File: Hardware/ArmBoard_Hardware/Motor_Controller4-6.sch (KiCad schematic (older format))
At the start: 27 parts

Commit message: ENx_# Updated
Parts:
- R?: value 3.3k -> 3.3
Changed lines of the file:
@@
 AR Path="/63845FEF/637AF810" Ref="R?"  Part="1"
 F 0 "R?" H 2559 4796 50  0000 L CNN
-F 1 "3.3k" H 2559 4705 50  0000 L CNN
+F 1 "3.3" H 2559 4705 50  0000 L CNN
 F 2 "" H 2500 4750 50  0001 C CNN
 F 3 "~" H 2500 4750 50  0001 C CNN

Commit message: Added MotorToggles
Removed extra schematic files, added a MotorToggle sheet for the toggle buttons, sheet docs were updated
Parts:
- gave numbers to parts that had none: 27

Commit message: need to change the mosfet and the other footrpints under it
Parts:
- R75: renamed from R68; footprint (none) -> Resistor_SMD:R_0603_1608Metric_Pad0.98x0.95mm_HandSolder
- R76: renamed from R69; footprint (none) -> Resistor_SMD:R_0603_1608Metric_Pad0.98x0.95mm_HandSolder
- R77: renamed from R70; footprint (none) -> Resistor_SMD:R_0603_1608Metric_Pad0.98x0.95mm_HandSolder
- R78: renamed from R71; footprint (none) -> Resistor_SMD:R_0603_1608Metric_Pad0.98x0.95mm_HandSolder
- R79: renamed from R72; footprint (none) -> Resistor_SMD:R_0603_1608Metric_Pad0.98x0.95mm_HandSolder
- R80: renamed from R73; footprint (none) -> Resistor_SMD:R_0603_1608Metric_Pad0.98x0.95mm_HandSolder
- R81: renamed from R74; footprint (none) -> Resistor_SMD:R_0603_1608Metric_Pad0.98x0.95mm_HandSolder
- R82: renamed from R75; footprint (none) -> Resistor_SMD:R_0603_1608Metric_Pad0.98x0.95mm_HandSolder
- R83: renamed from R76; footprint (none) -> Resistor_SMD:R_0603_1608Metric_Pad0.98x0.95mm_HandSolder
- R84: renamed from R77; footprint (none) -> Resistor_SMD:R_0603_1608Metric_Pad0.98x0.95mm_HandSolder
- R85: renamed from R78; footprint (none) -> Resistor_SMD:R_0603_1608Metric_Pad0.98x0.95mm_HandSolder
- R86: renamed from R79; footprint (none) -> Resistor_SMD:R_0603_1608Metric_Pad0.98x0.95mm_HandSolder
- R87: renamed from R80; footprint (none) -> Resistor_SMD:R_0603_1608Metric_Pad0.98x0.95mm_HandSolder
- R88: renamed from R81; footprint (none) -> Resistor_SMD:R_0603_1608Metric_Pad0.98x0.95mm_HandSolder
- R89: renamed from R82; footprint (none) -> Resistor_SMD:R_0603_1608Metric_Pad0.98x0.95mm_HandSolder
- R90: renamed from R83; footprint (none) -> Resistor_SMD:R_0603_1608Metric_Pad0.98x0.95mm_HandSolder
- R91: renamed from R84; footprint (none) -> Resistor_SMD:R_0603_1608Metric_Pad0.98x0.95mm_HandSolder
- R92: renamed from R85; footprint (none) -> Resistor_SMD:R_0603_1608Metric_Pad0.98x0.95mm_HandSolder
- R93: renamed from R86; footprint (none) -> Resistor_SMD:R_0603_1608Metric_Pad0.98x0.95mm_HandSolder
- R94: renamed from R87; footprint (none) -> Resistor_SMD:R_0603_1608Metric_Pad0.98x0.95mm_HandSolder
- R95: renamed from R88; footprint (none) -> Resistor_SMD:R_0603_1608Metric_Pad0.98x0.95mm_HandSolder
- U6: renamed from U7; footprint (none) -> MRDT_ICs:MultiPowerSO_30
- U7: renamed from U8; footprint (none) -> MRDT_ICs:MultiPowerSO_30
- U8: renamed from U9; footprint (none) -> MRDT_ICs:MultiPowerSO_30
- renumbered Q35 to Q34, Q36 to Q35, Q37 to Q36

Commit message: late night with the boy
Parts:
- removed Q34, Q35, Q36: BUK7M6R3-40EX, Package_TO_SOT_SMD:LFPAK33, symbol Transistor_FET:BUK7M6R3-40EX
- removed R75, R76, R77, R78, R79, R80, R81, R82, R83, R86, R88, R89, R90, R91, R92: 1k, Resistor_SMD:R_0603_1608Metric_Pad0.98x0.95mm_HandSolder, symbol Device:R_Small
- removed R84, R87, R93, R94, R95: 3.3k, Resistor_SMD:R_0603_1608Metric_Pad0.98x0.95mm_HandSolder, symbol Device:R_Small
- removed R85: 3.3, Resistor_SMD:R_0603_1608Metric_Pad0.98x0.95mm_HandSolder, symbol Device:R_Small
- removed U6, U7, U8: VNH5019A_E, MRDT_ICs:MultiPowerSO_30, symbol ArmBoard_Hardware-rescue:VNH5019A_E-MRDT_ICs
- added C10, C8, C9: C_Small, Capacitor_SMD:C_0603_1608Metric_Pad1.08x0.95mm_HandSolder, symbol Device:C_Small
- added R49, R50, R55: 20k, Resistor_SMD:R_0603_1608Metric_Pad0.98x0.95mm_HandSolder, symbol Device:R
- added R51, R52, R53, R54, R56, R57: 1k, Resistor_SMD:R_0603_1608Metric_Pad0.98x0.95mm_HandSolder, symbol Device:R_Small
- added U10, U11, U14: LTC6900, Package_TO_SOT_SMD:SOT-23-5_HandSoldering, symbol MRDT_Devices:LTC6900
- added U12, U13, U15: TB67H400AFNG,EL, MRDT_ICs:TB67H400AFNG,EL, symbol MRDT_ICs:TB67H400AFNG,EL
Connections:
- net labels added: +5V
- net labels removed: +3.3V, ENa_4, ENa_5, ENa_6, ENb_4, ENb_5, ENb_6
- wire segments 228 -> 165
- no-connect marks 0 -> 12

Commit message: Fixed Oscillators
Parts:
- U10, U11, U14: symbol MRDT_Devices:LTC6900 -> ArmBoard_Hardware-rescue:LTC6900-MRDT_Devices
- U12, U13, U15: symbol MRDT_ICs:TB67H400AFNG,EL -> ArmBoard_Hardware-rescue:TB67H400AFNG,EL-MRDT_ICs
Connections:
- net +5V: now also R49.1, R50.1, R55.1
- net GND: now also C10.2, C8.2, C9.2
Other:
- moved on the sheet: C10, C8, C9
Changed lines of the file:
@@
 IN_A_4
 $Comp
-L MRDT_ICs:TB67H400AFNG,EL U?
+L ArmBoard_Hardware-rescue:TB67H400AFNG,EL-MRDT_ICs U?
 U 1 1 624C6CB1
 P 3160 2365
@@
 	2135 1415 2360 1415
 $Comp
-L MRDT_Devices:LTC6900 U?
+L ArmBoard_Hardware-rescue:LTC6900-MRDT_Devices U?
 U 1 1 624C6C60
 P 1430 975
 AR Path="/63845F20/624C6C60" Ref="U?"  Part="1"
 AR Path="/63845FEF/624C6C60" Ref="U10"  Part="1"
+AR Path="/624C6C60" Ref="U10"  Part="1"
 F 0 "U10" H 1500 1260 50  0000 C CNN
 F 1 "LTC6900" H 1500 1169 50  0000 C CNN
@@
 L Device:C_Small C?
 U 1 1 624C6C44
-P 795 865
+P 675 865
 AR Path="/63845F20/624C6C44" Ref="C?"  Part="1"
 AR Path="/63845FEF/624C6C44" Ref="C8"  Part="1"
-F 0 "C8" H 887 911 50  0000 L CNN
-F 1 "C_Small" H 887 820 50  0000 L CNN
-F 2 "Capacitor_SMD:C_0603_1608Metric_Pad1.08x0.95mm_HandSolder" H 795 865 50  0001 C CNN
-F 3 "~" H 795 865 50  0001 C CNN
-	1    795  865
-	1    0    0    -1
-$EndComp
-Wire Wire Line
-	795  965  795  1115
+F 0 "C8" H 767 911 50  0000 L CNN
+F 1 "C_Small" H 767 820 50  0000 L CNN
+F 2 "Capacitor_SMD:C_0603_1608Metric_Pad1.08x0.95mm_HandSolder" H 675 865 50  0001 C CNN
+F 3 "~" H 675 865 50  0001 C CNN
+	1    675  865
+	1    0    0    -1
+$EndComp
 Wire Wire Line
 	795  1115 800  1115
@@
 Wire Wire Line
 	5950 1105 5955 1105
-Wire Wire Line
-	5950 955  5950 1105
 $Comp
 L Device:C_Small C?
 U 1 1 6250A179
-P 5950 855
+P 5830 865
 AR Path="/63845F20/6250A179" Ref="C?"  Part="1"
 AR Path="/63845FEF/6250A179" Ref="C10"  Part="1"
-F 0 "C10" H 6042 901 50  0000 L CNN
-F 1 "C_Small" H 6042 810 50  0000 L CNN
-F 2 "Capacitor_SMD:C_0603_1608Metric_Pad1.08x0.95mm_HandSolder" H 5950 855 50  0001 C CNN
-F 3 "~" H 5950 855 50  0001 C CNN
-	1    5950 855
+F 0 "C10" H 5922 911 50  0000 L CNN
+F 1 "C_Small" H 5922 820 50  0000 L CNN
+F 2 "Capacitor_SMD:C_0603_1608Metric_Pad1.08x0.95mm_HandSolder" H 5830 865 50  0001 C CNN
+F 3 "~" H 5830 865 50  0001 C CNN
+	1    5830 865
 	1    0    0    -1
 $EndComp
@@
 	6975 1005 7515 1005
 $Comp
-L MRDT_Devices:LTC6900 U?
+L ArmBoard_Hardware-rescue:LTC6900-MRDT_Devices U?
 U 1 1 6250A195
 P 6585 965
 AR Path="/63845F20/6250A195" Ref="U?"  Part="1"
 AR Path="/63845FEF/6250A195" Ref="U14"  Part="1"
+AR Path="/6250A195" Ref="U14"  Part="1"
 F 0 "U14" H 6655 1250 50  0000 C CNN
 F 1 "LTC6900" H 6655 1159 50  0000 C CNN
@@
 	8315 3905 8315 3780
 $Comp
-L MRDT_ICs:TB67H400AFNG,EL U?
+L ArmBoard_Hardware-rescue:TB67H400AFNG,EL-MRDT_ICs U?
 U 1 1 6250A1E6
 P 8315 2355
@@
 	1160 4480 1160 4445
 Wire Wire Line
-	950  4480 1160 4480
-Wire Wire Line
 	1335 4480 1335 4630
 $Comp
@@
 Wire Wire Line
 	950  4830 955  4830
-Wire Wire Line
-	950  4680 950  4830
 $Comp
 L Device:C_Small C?
 U 1 1 62512C8B
-P 950 4580
+P 830 4585
 AR Path="/63845F20/62512C8B" Ref="C?"  Part="1"
 AR Path="/63845FEF/62512C8B" Ref="C9"  Part="1"
-F 0 "C9" H 1042 4626 50  0000 L CNN
-F 1 "C_Small" H 1042 4535 50  0000 L CNN
-F 2 "Capacitor_SMD:C_0603_1608Metric_Pad1.08x0.95mm_HandSolder" H 950 4580 50  0001 C CNN
-F 3 "~" H 950 4580 50  0001 C CNN
-	1    950  4580
+F 0 "C9" H 922 4631 50  0000 L CNN
+F 1 "C_Small" H 922 4540 50  0000 L CNN
+F 2 "Capacitor_SMD:C_0603_1608Metric_Pad1.08x0.95mm_HandSolder" H 830 4585 50  0001 C CNN
+F 3 "~" H 830 4585 50  0001 C CNN
+	1    830  4585
 	1    0    0    -1
 $EndComp
@@
 	1975 4730 2515 4730
 $Comp
-L MRDT_Devices:LTC6900 U?
+L ArmBoard_Hardware-rescue:LTC6900-MRDT_Devices U?
 U 1 1 62512CA7
 P 1585 4690
 AR Path="/63845F20/62512CA7" Ref="U?"  Part="1"
 AR Path="/63845FEF/62512CA7" Ref="U11"  Part="1"
+AR Path="/62512CA7" Ref="U11"  Part="1"
 F 0 "U11" H 1655 4975 50  0000 C CNN
 F 1 "LTC6900" H 1655 4884 50  0000 C CNN
@@
 	3315 7630 3315 7505
 $Comp
-L MRDT_ICs:TB67H400AFNG,EL U?
+L ArmBoard_Hardware-rescue:TB67H400AFNG,EL-MRDT_ICs U?
 U 1 1 62512CF8
 P 3315 6080
@@
 Text GLabel 2365 6925 0    50   Output ~ 0
 OUTa_6
+Wire Wire Line
+	675  965  675  1015
+Wire Wire Line
+	795  765  795  1115
+Wire Wire Line
+	675  765  795  765
+Connection ~ 795  765
+Wire Wire Line
+	830  4485 830  4480
+Wire Wire Line
+	830  4480 950  4480
+Wire Wire Line
+	950  4480 950  4830
+Connection ~ 950  4480
+Wire Wire Line
+	950  4480 1160 4480
+Wire Wire Line
+	830  4685 830  4730
+Connection ~ 830  4730
+Connection ~ 675  1015
+Wire Wire Line
+	5830 765  5830 755
+Wire Wire Line
+	5830 755  5950 755
+Wire Wire Line
+	5950 755  5950 1105
+Connection ~ 5950 755
+Wire Wire Line
+	5830 965  5830 1005
+Connection ~ 5830 1005
 $EndSCHEMATC

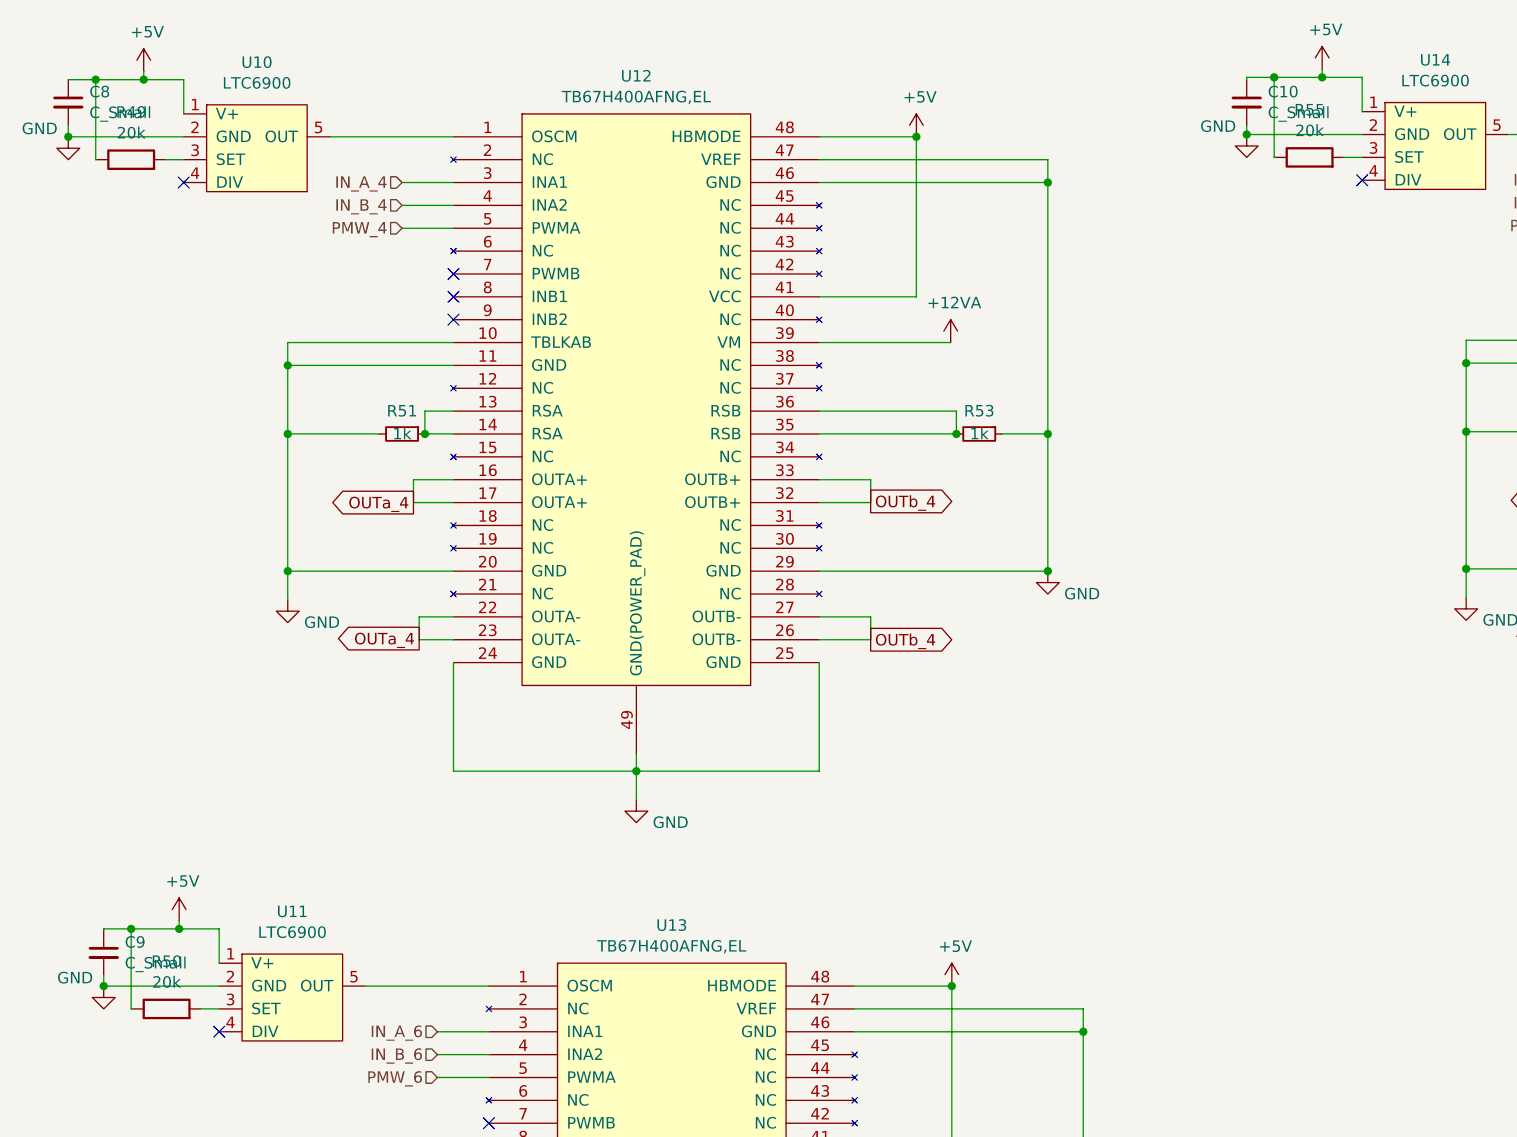
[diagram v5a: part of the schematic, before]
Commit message: Worked on Motor Drivers
added major tracing of motor drivers
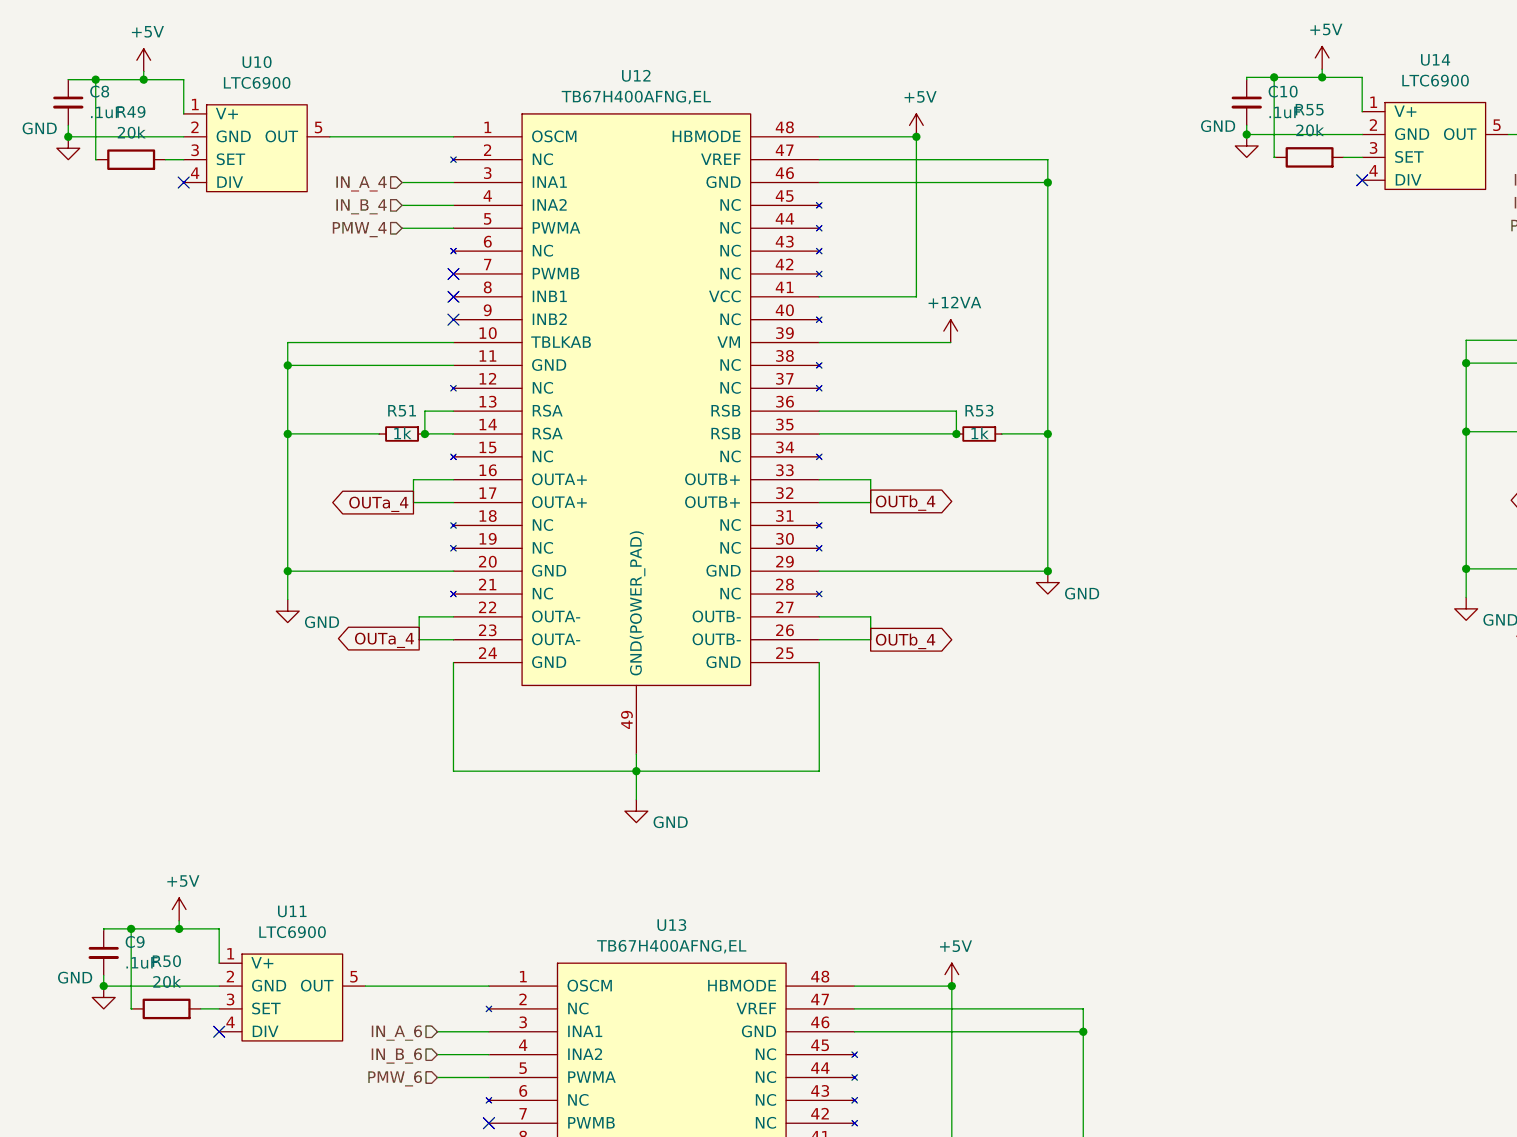
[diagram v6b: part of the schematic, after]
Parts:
- C10, C8, C9: value C_Small -> .1uF
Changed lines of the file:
@@
 AR Path="/63845FEF/624C6C44" Ref="C8"  Part="1"
 F 0 "C8" H 767 911 50  0000 L CNN
-F 1 "C_Small" H 767 820 50  0000 L CNN
+F 1 ".1uF" H 767 820 50  0000 L CNN
 F 2 "Capacitor_SMD:C_0603_1608Metric_Pad1.08x0.95mm_HandSolder" H 675 865 50  0001 C CNN
 F 3 "~" H 675 865 50  0001 C CNN
@@
 AR Path="/63845FEF/6250A179" Ref="C10"  Part="1"
 F 0 "C10" H 5922 911 50  0000 L CNN
-F 1 "C_Small" H 5922 820 50  0000 L CNN
+F 1 ".1uF" H 5922 820 50  0000 L CNN
 F 2 "Capacitor_SMD:C_0603_1608Metric_Pad1.08x0.95mm_HandSolder" H 5830 865 50  0001 C CNN
 F 3 "~" H 5830 865 50  0001 C CNN
@@
 AR Path="/63845FEF/62512C8B" Ref="C9"  Part="1"
 F 0 "C9" H 922 4631 50  0000 L CNN
-F 1 "C_Small" H 922 4540 50  0000 L CNN
+F 1 ".1uF" H 922 4540 50  0000 L CNN
 F 2 "Capacitor_SMD:C_0603_1608Metric_Pad1.08x0.95mm_HandSolder" H 830 4585 50  0001 C CNN
 F 3 "~" H 830 4585 50  0001 C CNN

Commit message: armboard review
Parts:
- removed C10, C8, C9: .1uF, Capacitor_SMD:C_0603_1608Metric_Pad1.08x0.95mm_HandSolder, symbol Device:C_Small
- removed R49, R50, R55: 20k, Resistor_SMD:R_0603_1608Metric_Pad0.98x0.95mm_HandSolder, symbol Device:R
- removed U10, U11, U14: LTC6900, Package_TO_SOT_SMD:SOT-23-5_HandSoldering, symbol ArmBoard_Hardware-rescue:LTC6900-MRDT_Devices
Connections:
- net OSC: now reaches U12.1 (OSCM)
- net OSC: now also U13.1 (OSCM), U15.1 (OSCM)
- no-connect marks 12 -> 9

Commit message: Rescued the Libaries
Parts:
- U12, U13, U15: symbol ArmBoard_Hardware-rescue:TB67H400AFNG,EL-MRDT_ICs -> MRDT_ICs:TB67H400AFNG,EL
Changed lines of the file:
@@
 IN_A_4
 $Comp
-L ArmBoard_Hardware-rescue:TB67H400AFNG,EL-MRDT_ICs U?
+L MRDT_ICs:TB67H400AFNG,EL U?
 U 1 1 624C6CB1
 P 3160 2365
 AR Path="/63845F20/624C6CB1" Ref="U?"  Part="1"
 AR Path="/63845FEF/624C6CB1" Ref="U12"  Part="1"
+AR Path="/624C6CB1" Ref="U12"  Part="1"
 F 0 "U12" H 3160 3980 50  0000 C CNN
 F 1 "TB67H400AFNG,EL" H 3160 3889 50  0000 C CNN
@@
 	8315 3905 8315 3780
 $Comp
-L ArmBoard_Hardware-rescue:TB67H400AFNG,EL-MRDT_ICs U?
+L MRDT_ICs:TB67H400AFNG,EL U?
 U 1 1 6250A1E6
 P 8315 2355
 AR Path="/63845F20/6250A1E6" Ref="U?"  Part="1"
 AR Path="/63845FEF/6250A1E6" Ref="U15"  Part="1"
+AR Path="/6250A1E6" Ref="U15"  Part="1"
 F 0 "U15" H 8315 3970 50  0000 C CNN
 F 1 "TB67H400AFNG,EL" H 8315 3879 50  0000 C CNN
@@
 	3315 7630 3315 7505
 $Comp
-L ArmBoard_Hardware-rescue:TB67H400AFNG,EL-MRDT_ICs U?
+L MRDT_ICs:TB67H400AFNG,EL U?
 U 1 1 62512CF8
 P 3315 6080
 AR Path="/63845F20/62512CF8" Ref="U?"  Part="1"
 AR Path="/63845FEF/62512CF8" Ref="U13"  Part="1"
+AR Path="/62512CF8" Ref="U13"  Part="1"
 F 0 "U13" H 3315 7695 50  0000 C CNN
 F 1 "TB67H400AFNG,EL" H 3315 7604 50  0000 C CNN
